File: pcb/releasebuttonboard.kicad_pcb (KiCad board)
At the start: 4 copper layers, 65 x 56 mm, 30 parts, among them SW1 ROTENC, U1 24C16, U2 RASPIPLUSHEADER, U3 OLEDHeader, U4 REncHeader, U5 BtnHeader, U6 PAM8407, U7 REncHeader

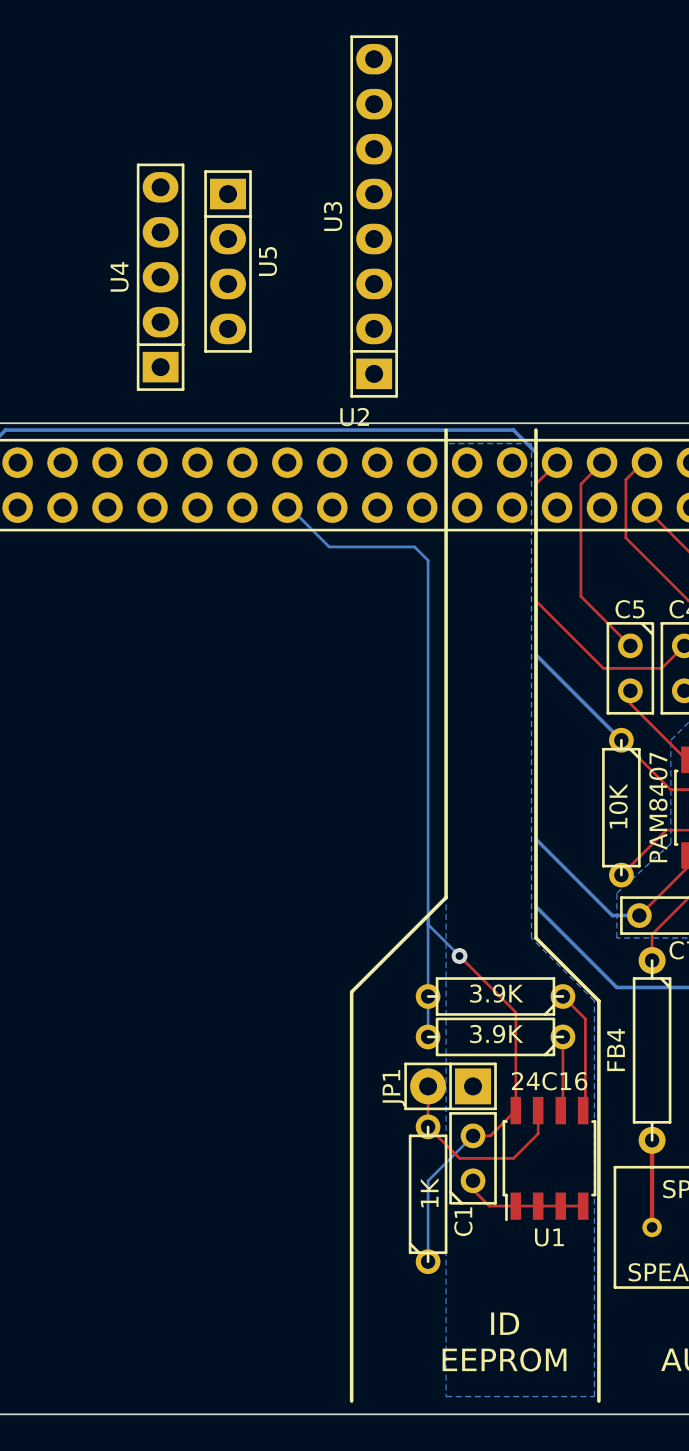
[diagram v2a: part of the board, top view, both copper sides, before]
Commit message: OLED header placement and routing.
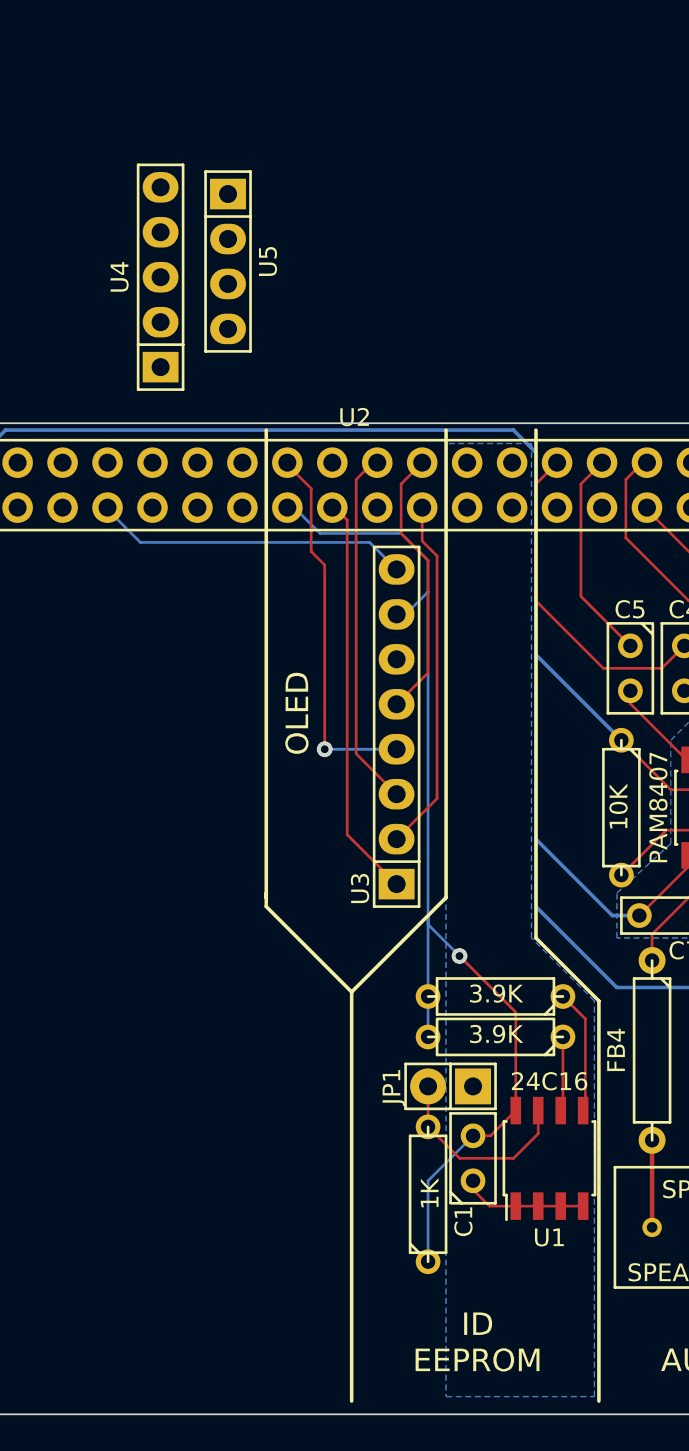
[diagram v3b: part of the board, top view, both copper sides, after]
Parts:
- moved U3 28.9 mm to (130.4, 85.2)
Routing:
- net /OLEDDATA: track 0.00 -> 22.9 mm
- net /OLEDRST: track 0.00 -> 21.1 mm, vias 0 -> 1
- net /OLEDDC: track 0.00 -> 20.3 mm
- net /OLEDCLK: track 0.00 -> 20.0 mm
- net GND: track 112.6 -> 130.5 mm
- net /OLEDCS: track 0.00 -> 15.5 mm
- net VCC: track 82.6 -> 85.1 mm
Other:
- board text added: "OLED"
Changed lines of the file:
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@@
   (general
     (links 76)
-    (no_connects 24)
+    (no_connects 17)
     (area 95.449999 67.949999 160.550001 124.050001)
     (thickness 1.6)
-    (drawings 21)
-    (tracks 153)
+    (drawings 26)
+    (tracks 186)
     (zones 0)
     (modules 30)
@@
   )
   (module Pin_Headers:Pin_Header_Straight_1x08 (layer F.Cu)
-    (at 129.094 56.323 90)
+    (at 130.364 85.152 90)
     (descr "Through hole pin header")
     (tags "pin header")
-    (fp_text reference U3 (at 0 -2.286 90) (layer F.SilkS)
-      (effects (font (size 1 1) (thickness 0.15)))
-    )
-    (fp_text value OLEDHeader (at 0 0 90) (layer F.SilkS) hide
+    (fp_text reference U3 (at -9.144 -2.032 90) (layer F.SilkS)
+      (effects (font (size 1 1) (thickness 0.15)))
+    )
+    (fp_text value OLEDHeader (at -2.54 -2.032 90) (layer F.SilkS) hide
       (effects (font (size 1 1) (thickness 0.15)))
     )
@@
     (pad 1 thru_hole circle (at 0 0) (size 6.2 6.2) (drill 2.75) (layers *.Cu *.Mask F.SilkS))
   )
+  (gr_line (start 122.998 94.804) (end 122.998 94.55) (angle 90) (layer F.SilkS) (width 0.2))
+  (gr_line (start 122.998 95.312) (end 122.998 94.804) (angle 90) (layer F.SilkS) (width 0.2))
+  (gr_line (start 127.824 100.138) (end 122.998 95.312) (angle 90) (layer F.SilkS) (width 0.2))
+  (gr_line (start 122.998 68.388) (end 122.998 94.804) (angle 90) (layer F.SilkS) (width 0.2))
+  (gr_text OLED (at 124.776 84.39 90) (layer F.SilkS)
+    (effects (font (thickness 0.1905)))
+  )
   (gr_line (start 133.158 94.804) (end 133.158 68.388) (angle 90) (layer F.SilkS) (width 0.2))
   (gr_line (start 127.824 100.138) (end 133.158 94.804) (angle 90) (layer F.SilkS) (width 0.2))
   (gr_line (start 127.824 123.252) (end 127.824 100.138) (angle 90) (layer F.SilkS) (width 0.2))
-  (gr_text "ID\nEEPROM" (at 136.46 119.95) (layer F.SilkS)
+  (gr_text "ID\nEEPROM" (at 134.936 119.95) (layer F.SilkS)
     (effects (font (thickness 0.1905)))
   )
@@
   (gr_line (start 95.5 71) (end 95.5 121) (angle 90) (layer Edge.Cuts) (width 0.1))
   (gr_arc (start 98.5 71) (end 95.5 71) (angle 90) (layer Edge.Cuts) (width 0.1))
+  (segment (start 114.03 72.77) (end 114.03 72.882) (width 0.1524) (layer B.Cu) (net 1))
+  (segment (start 114.03 72.882) (end 115.886 74.738) (width 0.1524) (layer B.Cu) (net 1))
+  (segment (start 128.84 74.738) (end 130.364 76.262) (width 0.1524) (layer B.Cu) (net 1))
+  (segment (start 115.886 74.738) (end 128.84 74.738) (width 0.1524) (layer B.Cu) (net 1))
   (segment (start 139.635 112.236) (end 140.905 112.236) (width 0.1524) (layer F.Cu) (net 1))
   (segment (start 138.365 112.236) (end 139.635 112.236) (width 0.1524) (layer F.Cu) (net 1))
@@
   (segment (start 150.557 92.424) (end 150.557 94.423) (width 0.1524) (layer F.Cu) (net 1))
   (segment (start 150.557 94.423) (end 149.16 95.82) (width 0.1524) (layer F.Cu) (net 1))
+  (segment (start 130.364 78.802) (end 130.872 78.802) (width 0.1524) (layer B.Cu) (net 2))
+  (segment (start 130.872 78.802) (end 132.142 77.532) (width 0.1524) (layer B.Cu) (net 2))
+  (segment (start 124.19 72.77) (end 124.586 72.77) (width 0.1524) (layer B.Cu) (net 2))
+  (segment (start 124.586 72.77) (end 126.046 74.23) (width 0.1524) (layer B.Cu) (net 2))
+  (segment (start 132.142 75.754) (end 132.142 77.532) (width 0.1524) (layer B.Cu) (net 2))
+  (segment (start 132.142 77.532) (end 132.142 95.82) (width 0.1524) (layer B.Cu) (net 2))
+  (segment (start 130.618 74.23) (end 132.142 75.754) (width 0.1524) (layer B.Cu) (net 2))
+  (segment (start 126.046 74.23) (end 130.618 74.23) (width 0.1524) (layer B.Cu) (net 2))
   (segment (start 132.142 95.82) (end 132.142 96.328) (width 0.1524) (layer B.Cu) (net 2))
   (segment (start 137.095 101.281) (end 137.095 106.836) (width 0.1524) (layer F.Cu) (net 2))
@@
   (segment (start 132.142 100.392) (end 132.142 102.678) (width 0.1524) (layer B.Cu) (net 2))
   (segment (start 124.19 72.77) (end 124.332 72.77) (width 0.1524) (layer B.Cu) (net 2))
-  (segment (start 124.332 72.77) (end 126.554 74.992) (width 0.1524) (layer B.Cu) (net 2))
-  (segment (start 132.142 75.754) (end 132.142 95.82) (width 0.1524) (layer B.Cu) (net 2))
   (segment (start 132.142 95.82) (end 132.142 100.392) (width 0.1524) (layer B.Cu) (net 2))
-  (segment (start 131.38 74.992) (end 132.142 75.754) (width 0.1524) (layer B.Cu) (net 2))
-  (segment (start 126.554 74.992) (end 131.38 74.992) (width 0.1524) (layer B.Cu) (net 2))
   (segment (start 132.142 115.378) (end 132.142 110.806) (width 0.1524) (layer B.Cu) (net 2))
   (segment (start 132.142 110.806) (end 134.682 108.266) (width 0.1524) (layer B.Cu) (net 2))
@@
   (segment (start 151.192 90.994) (end 153.097 89.089) (width 0.1524) (layer F.Cu) (net 20))
   (segment (start 145.604 90.994) (end 151.192 90.994) (width 0.1524) (layer F.Cu) (net 20))
+  (segment (start 124.19 70.23) (end 124.19 70.342) (width 0.1524) (layer F.Cu) (net 26))
+  (segment (start 124.19 70.342) (end 125.538 71.69) (width 0.1524) (layer F.Cu) (net 26))
+  (segment (start 125.538 71.69) (end 125.538 75.246) (width 0.1524) (layer F.Cu) (net 26))
+  (segment (start 125.538 75.246) (end 126.3 76.008) (width 0.1524) (layer F.Cu) (net 26))
+  (segment (start 126.3 76.008) (end 126.3 86.422) (width 0.1524) (layer F.Cu) (net 26))
+  (via (at 126.3 86.422) (size 0.889) (layers F.Cu B.Cu) (net 26))
+  (segment (start 126.3 86.422) (end 130.364 86.422) (width 0.1524) (layer B.Cu) (net 26))
+  (segment (start 129.27 70.23) (end 129.03 70.23) (width 0.1524) (layer F.Cu) (net 27))
+  (segment (start 129.03 70.23) (end 128.078 71.182) (width 0.1524) (layer F.Cu) (net 27))
+  (segment (start 128.078 71.182) (end 128.078 86.676) (width 0.1524) (layer F.Cu) (net 27))
+  (segment (start 128.078 86.676) (end 130.364 88.962) (width 0.1524) (layer F.Cu) (net 27))
+  (segment (start 126.73 72.77) (end 126.872 72.77) (width 0.1524) (layer F.Cu) (net 31))
+  (segment (start 126.872 72.77) (end 127.57 73.468) (width 0.1524) (layer F.Cu) (net 31))
+  (segment (start 127.57 73.468) (end 127.57 91.248) (width 0.1524) (layer F.Cu) (net 31))
+  (segment (start 127.57 91.248) (end 130.364 94.042) (width 0.1524) (layer F.Cu) (net 31))
+  (segment (start 131.81 72.77) (end 131.81 74.66) (width 0.1524) (layer F.Cu) (net 33))
+  (segment (start 132.65 89.216) (end 130.364 91.502) (width 0.1524) (layer F.Cu) (net 33))
+  (segment (start 132.65 75.5) (end 132.65 89.216) (width 0.1524) (layer F.Cu) (net 33))
+  (segment (start 131.81 74.66) (end 132.65 75.5) (width 0.1524) (layer F.Cu) (net 33))
+  (segment (start 131.81 70.23) (end 131.81 70.244) (width 0.1524) (layer F.Cu) (net 34))
+  (segment (start 131.81 70.244) (end 130.618 71.436) (width 0.1524) (layer F.Cu) (net 34))
+  (segment (start 130.618 71.436) (end 130.618 74.23) (width 0.1524) (layer F.Cu) (net 34))
+  (segment (start 130.618 74.23) (end 132.142 75.754) (width 0.1524) (layer F.Cu) (net 34))
+  (segment (start 132.142 75.754) (end 132.142 82.104) (width 0.1524) (layer F.Cu) (net 34))
+  (segment (start 132.142 82.104) (end 130.364 83.882) (width 0.1524) (layer F.Cu) (net 34))
   (segment (start 103.87 70.23) (end 106.41 70.23) (width 0.1524) (layer In1.Cu) (net 36))
   (segment (start 138.238 91.502) (end 138.238 95.312) (width 0.2032) (layer B.Cu) (net 36))

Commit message: Connect the ID EEPROM data pins.
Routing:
- net /ID_SC: track 4.22 -> 38.8 mm
- net /ID_SD: track 7.02 -> 35.8 mm
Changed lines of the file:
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@@
   (general
     (links 76)
-    (no_connects 17)
+    (no_connects 16)
     (area 95.449999 67.949999 160.550001 124.050001)
     (thickness 1.6)
     (drawings 26)
-    (tracks 186)
+    (tracks 191)
     (zones 0)
     (modules 30)
@@
   (segment (start 136.968 109.536) (end 138.365 108.139) (width 0.1524) (layer F.Cu) (net 17))
   (segment (start 133.92 109.536) (end 136.968 109.536) (width 0.1524) (layer F.Cu) (net 17))
+  (segment (start 136.89 72.77) (end 136.89 97.52) (width 0.1524) (layer F.Cu) (net 18) (status 400000))
+  (segment (start 136.89 97.52) (end 139.762 100.392) (width 0.1524) (layer F.Cu) (net 18) (status 800000))
   (segment (start 139.762 100.392) (end 141.032 101.662) (width 0.1524) (layer F.Cu) (net 18))
   (segment (start 141.032 101.662) (end 141.032 106.709) (width 0.1524) (layer F.Cu) (net 18))
   (segment (start 141.032 106.709) (end 140.905 106.836) (width 0.1524) (layer F.Cu) (net 18))
+  (segment (start 136.89 70.23) (end 136.89 70.244) (width 0.1524) (layer F.Cu) (net 19) (status C00000))
+  (segment (start 136.89 70.244) (end 135.698 71.436) (width 0.1524) (layer F.Cu) (net 19) (status 400000))
+  (segment (start 135.698 98.614) (end 139.762 102.678) (width 0.1524) (layer F.Cu) (net 19) (status 800000))
+  (segment (start 135.698 71.436) (end 135.698 98.614) (width 0.1524) (layer F.Cu) (net 19))
   (segment (start 139.762 102.678) (end 139.762 106.709) (width 0.1524) (layer F.Cu) (net 19))
   (segment (start 139.762 106.709) (end 139.635 106.836) (width 0.1524) (layer F.Cu) (net 19))
-  (segment (start 136.89 70.23) (end 136.89 70.244) (width 0.1524) (layer F.Cu) (net 19))
   (segment (start 143.064 93.534) (end 145.604 90.994) (width 0.1524) (layer F.Cu) (net 20))
   (segment (start 153.097 89.089) (end 153.097 87.024) (width 0.1524) (layer F.Cu) (net 20))

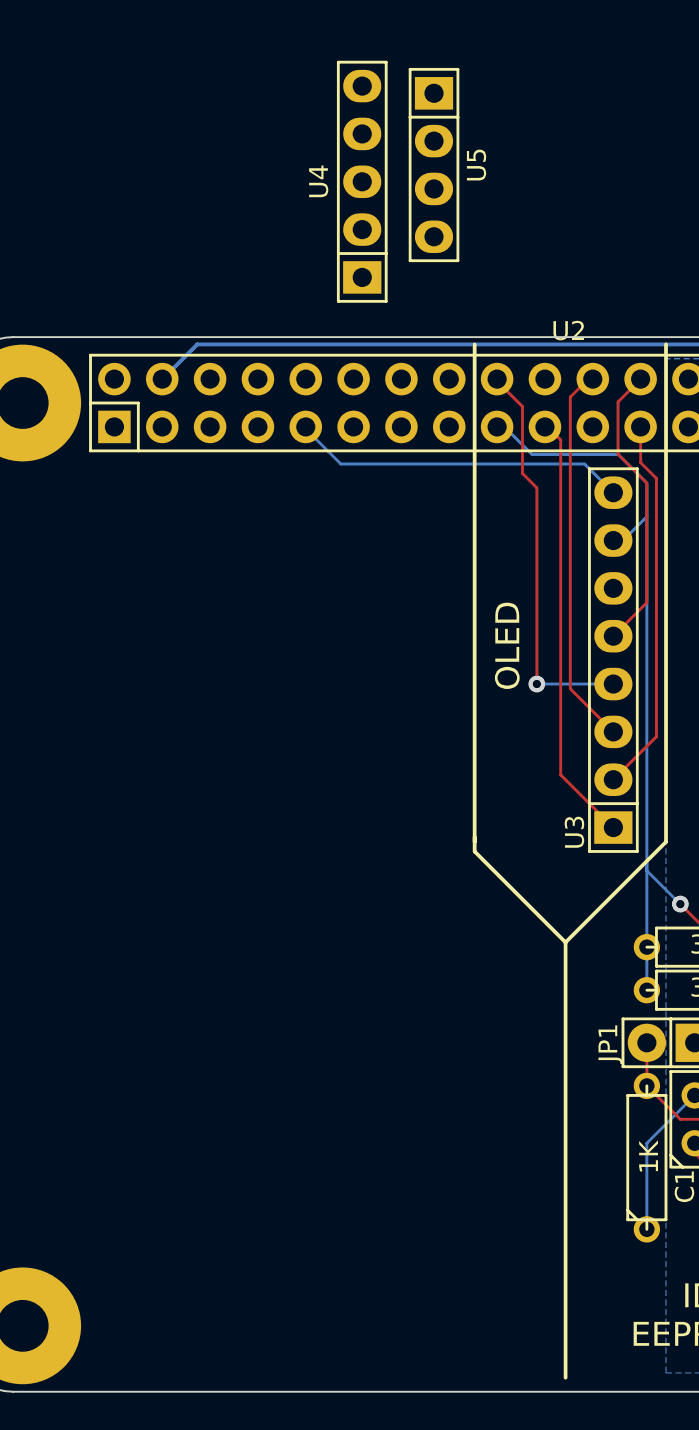
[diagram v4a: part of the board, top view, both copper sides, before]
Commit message: Button and rotary encoder header placement and tracks.
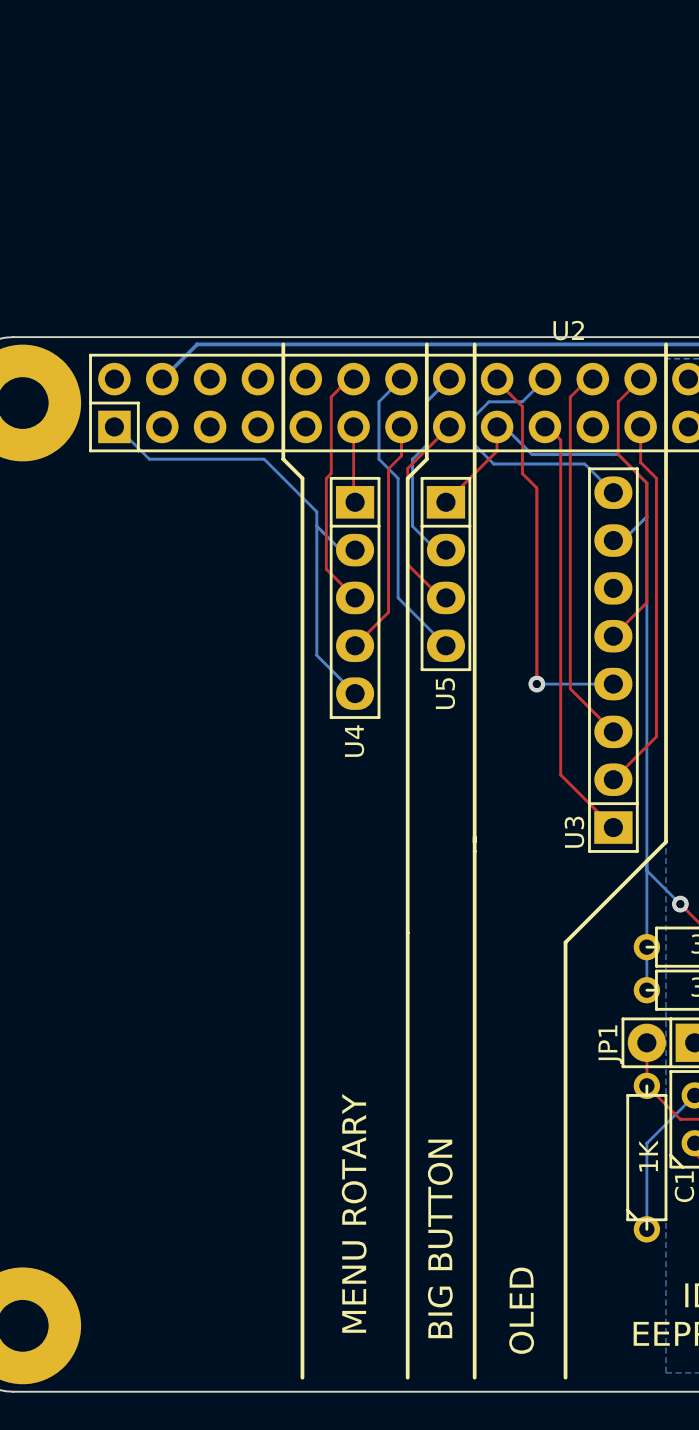
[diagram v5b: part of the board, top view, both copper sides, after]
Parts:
- moved U4 22.1 mm to (116.6, 81.8), turned to 270 degrees
- moved U5 21.7 mm to (121.5, 80.6)
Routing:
- net VCC: track 85.1 -> 115.7 mm
- net /MNUROTB: track 0.00 -> 13.0 mm
- net GND: track 130.5 -> 143.4 mm
- net /MNUPUSH: track 0.00 -> 12.6 mm
- net /BTNLED: track 0.00 -> 11.0 mm
- net /BTNPUSH: track 0.00 -> 10.9 mm
- net /MNUROTA: track 0.00 -> 4.03 mm
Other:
- board text added: "BIG BUTTON"
- board text added: "MENU ROTARY"
